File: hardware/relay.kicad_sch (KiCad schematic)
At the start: 4 parts, among them K1 G5Q-1, U2 TCMT1100

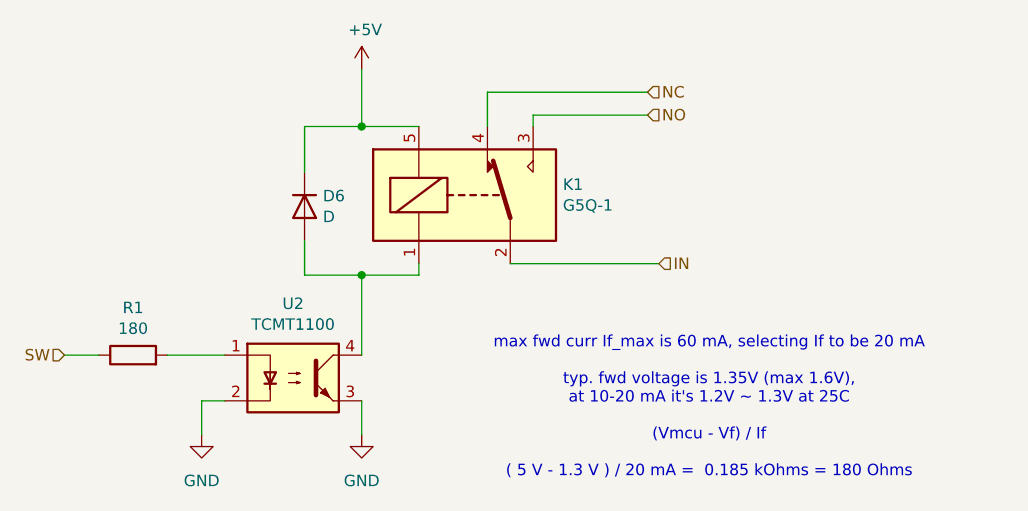
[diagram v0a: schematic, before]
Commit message: update to use latest kmlib; needs revision for connectors and ground inputs on analog inputs
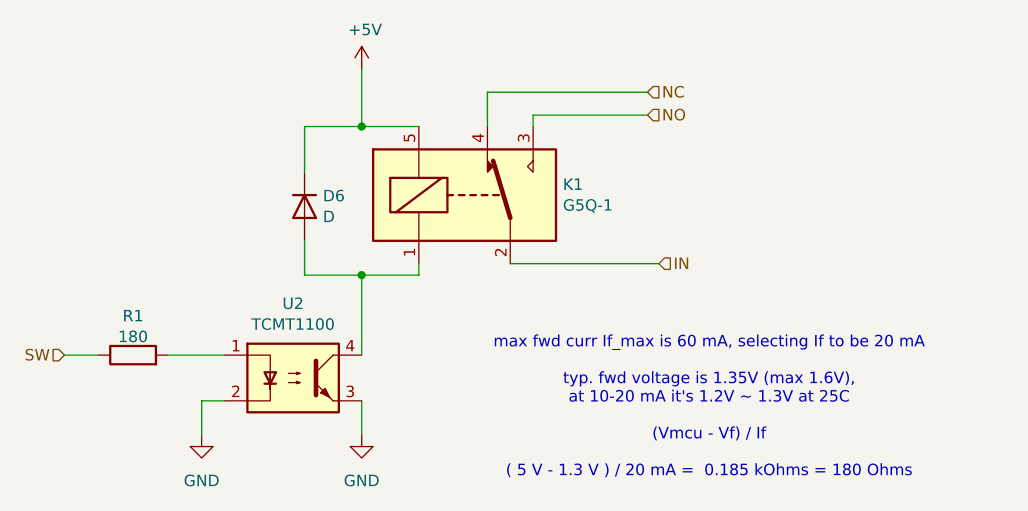
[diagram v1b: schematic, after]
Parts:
- R1: symbol BREAD_Slice-rescue:R-OCI_UPL_1_Resistors -> Device:R
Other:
- moved on the sheet: R1
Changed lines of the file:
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@@
 			)
 		)
-		(property "Description" ""
+		(property "Description" "Optocoupler, Vce 70V, CTR 50-600%, Viso 3750V (RMS), SOP-4"
 			(at 137.16 88.9 0)
 			(effects
@@
 		(on_board yes)
 		(dnp no)
-		(property "Reference" "#PWR024"
+		(property "Reference" "#PWR022"
 			(at 127 101.6 0)
 			(effects
@@
 			)
 		)
-		(property "Description" ""
+		(property "Description" "Power symbol creates a global label with name \"GND\" , ground"
 			(at 127 95.25 0)
 			(effects
@@
 			(project "BREAD_Slice"
 				(path "/66043bca-a260-4915-9fce-8a51d324c687/8f59afdc-92bc-4963-a20c-70846ea17764"
-					(reference "#PWR030")
-					(unit 1)
-				)
-				(path "/66043bca-a260-4915-9fce-8a51d324c687/b9db80e2-f72b-4f99-aaab-326ee1ac6c8c"
-					(reference "#PWR027")
-					(unit 1)
-				)
-				(path "/66043bca-a260-4915-9fce-8a51d324c687/ef5264c1-9ff0-4631-9d8a-028757371869"
-					(reference "#PWR024")
-					(unit 1)
-				)
-				(path "/66043bca-a260-4915-9fce-8a51d324c687/f28cb47c-42cc-4288-a9dc-34f5a078f400"
-					(reference "#PWR033")
+					(reference "#PWR028")
+					(unit 1)
+				)
+				(path "/66043bca-a260-4915-9fce-8a51d324c687/b9db80e2-f72b-4f99-aaab-326ee1ac6c8c"
+					(reference "#PWR025")
+					(unit 1)
+				)
+				(path "/66043bca-a260-4915-9fce-8a51d324c687/ef5264c1-9ff0-4631-9d8a-028757371869"
+					(reference "#PWR022")
+					(unit 1)
+				)
+				(path "/66043bca-a260-4915-9fce-8a51d324c687/f28cb47c-42cc-4288-a9dc-34f5a078f400"
+					(reference "#PWR031")
 					(unit 1)
 				)
@@
 		(on_board yes)
 		(dnp no)
-		(property "Reference" "#PWR025"
+		(property "Reference" "#PWR023"
 			(at 144.78 58.42 0)
 			(effects
@@
 			)
 		)
-		(property "Description" ""
+		(property "Description" "Power symbol creates a global label with name \"+5V\""
 			(at 144.78 54.61 0)
 			(effects
@@
 			(project "BREAD_Slice"
 				(path "/66043bca-a260-4915-9fce-8a51d324c687/8f59afdc-92bc-4963-a20c-70846ea17764"
-					(reference "#PWR031")
-					(unit 1)
-				)
-				(path "/66043bca-a260-4915-9fce-8a51d324c687/b9db80e2-f72b-4f99-aaab-326ee1ac6c8c"
-					(reference "#PWR028")
-					(unit 1)
-				)
-				(path "/66043bca-a260-4915-9fce-8a51d324c687/ef5264c1-9ff0-4631-9d8a-028757371869"
-					(reference "#PWR025")
-					(unit 1)
-				)
-				(path "/66043bca-a260-4915-9fce-8a51d324c687/f28cb47c-42cc-4288-a9dc-34f5a078f400"
-					(reference "#PWR034")
+					(reference "#PWR029")
+					(unit 1)
+				)
+				(path "/66043bca-a260-4915-9fce-8a51d324c687/b9db80e2-f72b-4f99-aaab-326ee1ac6c8c"
+					(reference "#PWR026")
+					(unit 1)
+				)
+				(path "/66043bca-a260-4915-9fce-8a51d324c687/ef5264c1-9ff0-4631-9d8a-028757371869"
+					(reference "#PWR023")
+					(unit 1)
+				)
+				(path "/66043bca-a260-4915-9fce-8a51d324c687/f28cb47c-42cc-4288-a9dc-34f5a078f400"
+					(reference "#PWR032")
 					(unit 1)
 				)
@@
 		(on_board yes)
 		(dnp no)
-		(property "Reference" "#PWR026"
+		(property "Reference" "#PWR024"
 			(at 144.78 101.6 0)
 			(effects
@@
 			)
 		)
-		(property "Description" ""
+		(property "Description" "Power symbol creates a global label with name \"GND\" , ground"
 			(at 144.78 95.25 0)
 			(effects
@@
 			(project "BREAD_Slice"
 				(path "/66043bca-a260-4915-9fce-8a51d324c687/8f59afdc-92bc-4963-a20c-70846ea17764"
-					(reference "#PWR032")
-					(unit 1)
-				)
-				(path "/66043bca-a260-4915-9fce-8a51d324c687/b9db80e2-f72b-4f99-aaab-326ee1ac6c8c"
-					(reference "#PWR029")
-					(unit 1)
-				)
-				(path "/66043bca-a260-4915-9fce-8a51d324c687/ef5264c1-9ff0-4631-9d8a-028757371869"
-					(reference "#PWR026")
-					(unit 1)
-				)
-				(path "/66043bca-a260-4915-9fce-8a51d324c687/f28cb47c-42cc-4288-a9dc-34f5a078f400"
-					(reference "#PWR035")
+					(reference "#PWR030")
+					(unit 1)
+				)
+				(path "/66043bca-a260-4915-9fce-8a51d324c687/b9db80e2-f72b-4f99-aaab-326ee1ac6c8c"
+					(reference "#PWR027")
+					(unit 1)
+				)
+				(path "/66043bca-a260-4915-9fce-8a51d324c687/ef5264c1-9ff0-4631-9d8a-028757371869"
+					(reference "#PWR024")
+					(unit 1)
+				)
+				(path "/66043bca-a260-4915-9fce-8a51d324c687/f28cb47c-42cc-4288-a9dc-34f5a078f400"
+					(reference "#PWR033")
 					(unit 1)
 				)
@@
 			)
 		)
-		(property "Description" ""
+		(property "Description" "Diode"
 			(at 138.43 69.85 0)
 			(effects
@@
 			)
 		)
+		(property "Sim.Device" "D"
+			(at 138.43 69.85 0)
+			(effects
+				(font
+					(size 1.27 1.27)
+				)
+				(hide yes)
+			)
+		)
+		(property "Sim.Pins" "1=K 2=A"
+			(at 138.43 69.85 0)
+			(effects
+				(font
+					(size 1.27 1.27)
+				)
+				(hide yes)
+			)
+		)
 		(pin "1"
 		)
@@
 	)
 	(symbol
-		(lib_id "BREAD_Slice-rescue:R-OCI_UPL_1_Resistors")
-		(at 119.38 86.36 0)
+		(lib_id "Device:R")
+		(at 119.38 86.36 90)
 		(unit 1)
 		(exclude_from_sim no)
@@
 		(dnp no)
 		(property "Reference" "R1"
-			(at 119.38 81.1022 0)
+			(at 119.38 82.0166 90)
 			(effects
 				(font
@@
 		)
 		(property "Value" "180"
-			(at 119.38 83.4136 0)
+			(at 119.38 84.328 90)
 			(effects
 				(font
@@
 		)
 		(property "Footprint" "Resistor_SMD:R_1206_3216Metric_Pad1.30x1.75mm_HandSolder"
-			(at 119.38 88.138 0)
-			(effects
-				(font
-					(size 1.27 1.27)
-				)
-				(hide yes)
-			)
-		)
-		(property "Datasheet" ""
-			(at 119.38 86.36 90)
-			(effects
-				(font
-					(size 1.27 1.27)
-				)
-			)
-		)
-		(property "Description" ""
+			(at 119.38 88.138 90)
+			(effects
+				(font
+					(size 1.27 1.27)
+				)
+				(hide yes)
+			)
+		)
+		(property "Datasheet" "~"
+			(at 119.38 86.36 0)
+			(effects
+				(font
+					(size 1.27 1.27)
+				)
+				(hide yes)
+			)
+		)
+		(property "Description" "Resistor"
 			(at 119.38 86.36 0)
 			(effects
@@
 			)
 		)
-		(property "Description" ""
+		(property "Description" "Omron G5G relay, Miniature Single Pole, SPDT, 10A"
 			(at 156.21 68.58 0)
 			(effects
